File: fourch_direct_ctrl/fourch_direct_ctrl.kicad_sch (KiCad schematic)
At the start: 53 parts, among them J1 Conn_01x04, J10 Conn_01x01, J11 Conn_01x01, J12 Conn_01x01, J13 Conn_01x01, J14 Conn_01x01, J15 Conn_01x01, J16 Conn_01x01, J17 Conn_01x01, J2 Conn_01x02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

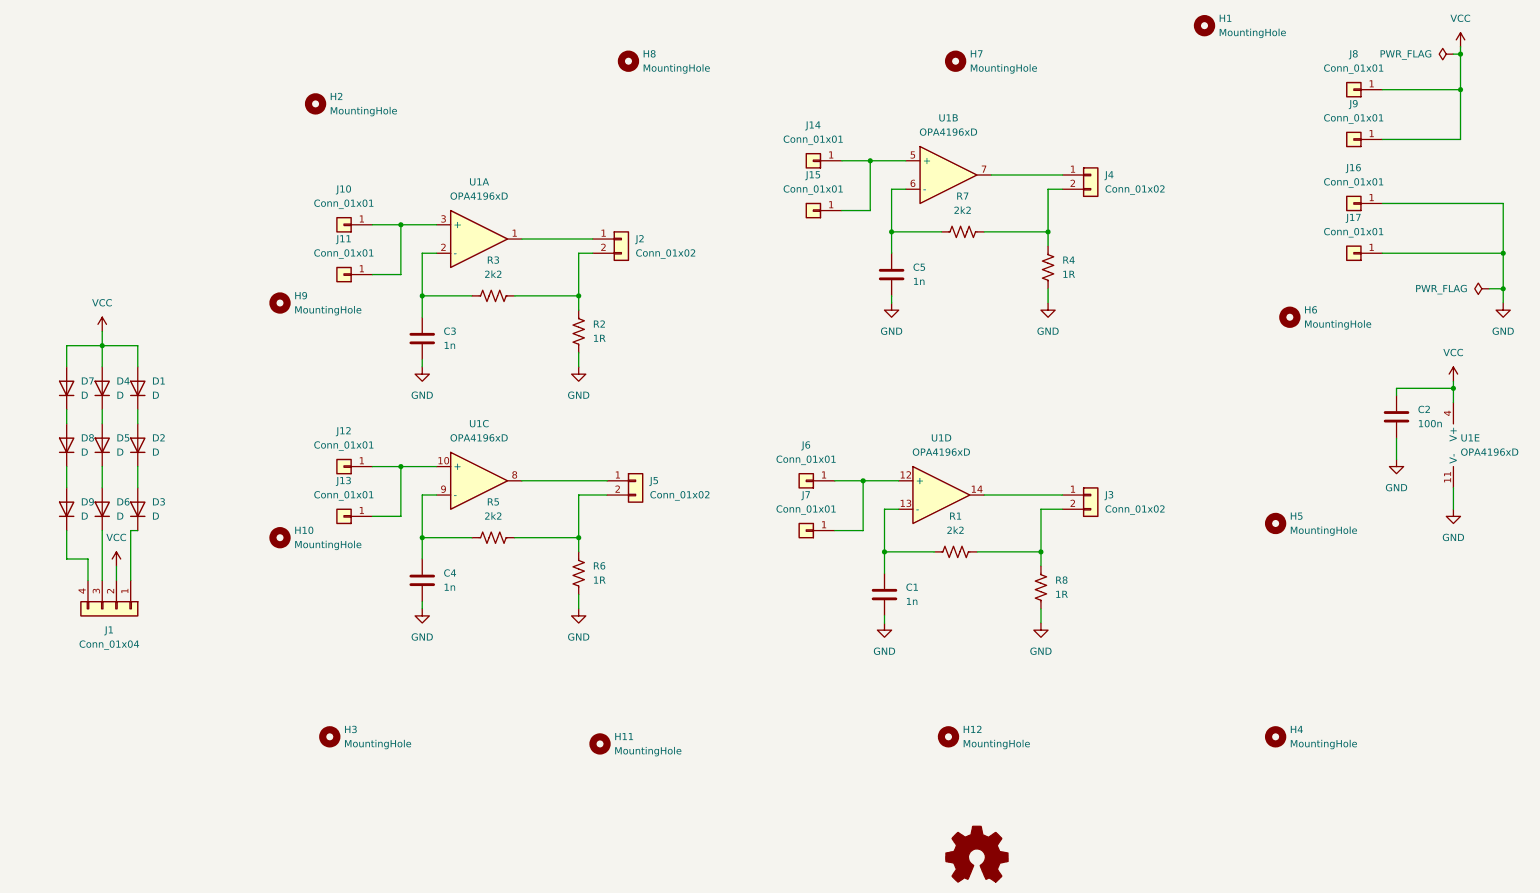
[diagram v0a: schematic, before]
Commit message: rev up fourch lights, add distroboard
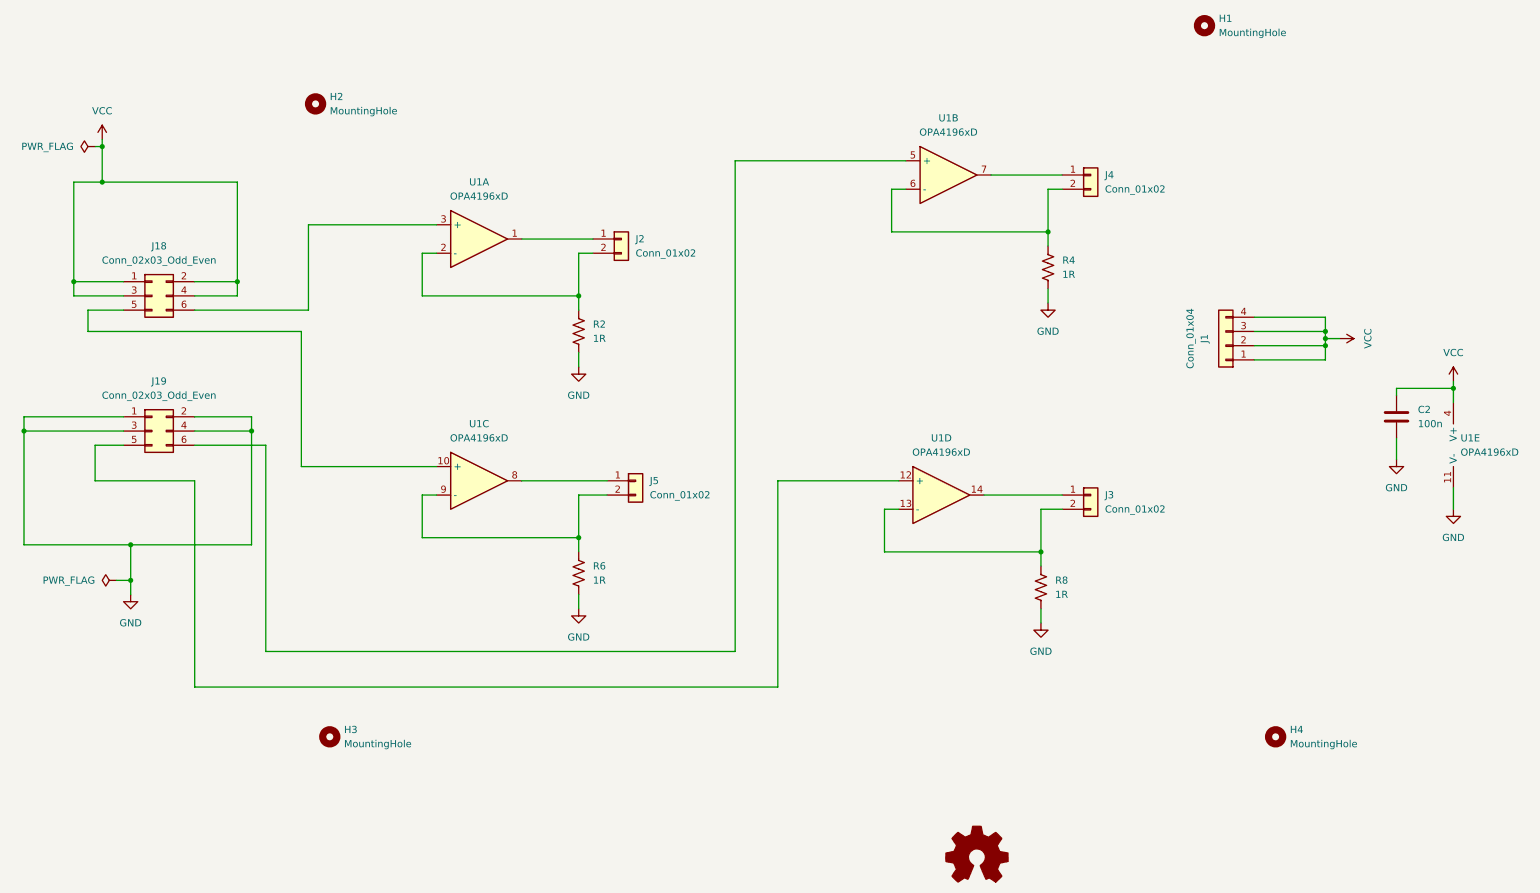
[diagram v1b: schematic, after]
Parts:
- removed C1, C3, C4, C5: 1n, Capacitor_SMD:C_0805_2012Metric_Pad1.18x1.45mm_HandSolder, symbol Device:C
- removed D1, D2, D3, D4, D5, D6, D7, D8, D9: D, Diode_SMD:D_SOD-123F, symbol Device:D
- removed H10, H11, H12, H5, H6, H7, H8, H9: MountingHole, custom_footprints:MountingHole_4.2mm, symbol Mechanical:MountingHole
- removed J10, J11, J12, J13, J14, J15, J6, J7: Conn_01x01, custom_footprints:TE_2834010-3_1x01_P3.0mm_Horizontal, symbol Connector_Generic:Conn_01x01
- removed J16, J17, J8, J9: Conn_01x01, custom_footprints:TE_2834012-3_1x01_P4.0mm_Horizontal, symbol Connector_Generic:Conn_01x01
- removed R1, R3, R5, R7: 2k2, Resistor_SMD:R_0805_2012Metric_Pad1.20x1.40mm_HandSolder, symbol Device:R_US
- added J18, J19: Conn_02x03_Odd_Even, Connector_Wuerth:Wuerth_WR-PHD_610006243021_SMD_2x03_P2.54mm_Vertical, symbol Connector_Generic:Conn_02x03_Odd_Even
- H1, H2, H3, H4: footprint custom_footprints:MountingHole_3.0mm -> custom_footprints:MountingHole_3.45mm
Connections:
- net GND: now also J19.1 (Pin_1), J19.2 (Pin_2), J19.3 (Pin_3), J19.4 (Pin_4)
- net VCC: now also J1.1 (Pin_1), J1.3 (Pin_3), J1.4 (Pin_4), J18.1 (Pin_1), J18.2 (Pin_2), J18.3 (Pin_3), J18.4 (Pin_4)
- net at U1.5 (+): now also J19.6 (Pin_6)
- net at U1.6 (-): now also J4.2 (Pin_2), R4.1
- net at U1.3 (+): now also J18.6 (Pin_6)
- net at U1.13 (-): now also J3.2 (Pin_2), R8.1
- net at U1.10 (+): now also J18.5 (Pin_5)
- net at U1.9 (-): now also J5.2 (Pin_2), R6.1
- net at J2.2 (Pin_2), R2.1: now also U1.2 (-)
- net at U1.12 (+): now also J19.5 (Pin_5)
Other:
- moved on the sheet: J1

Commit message: switch opamps to dual flavors, build in on-board TEC current control
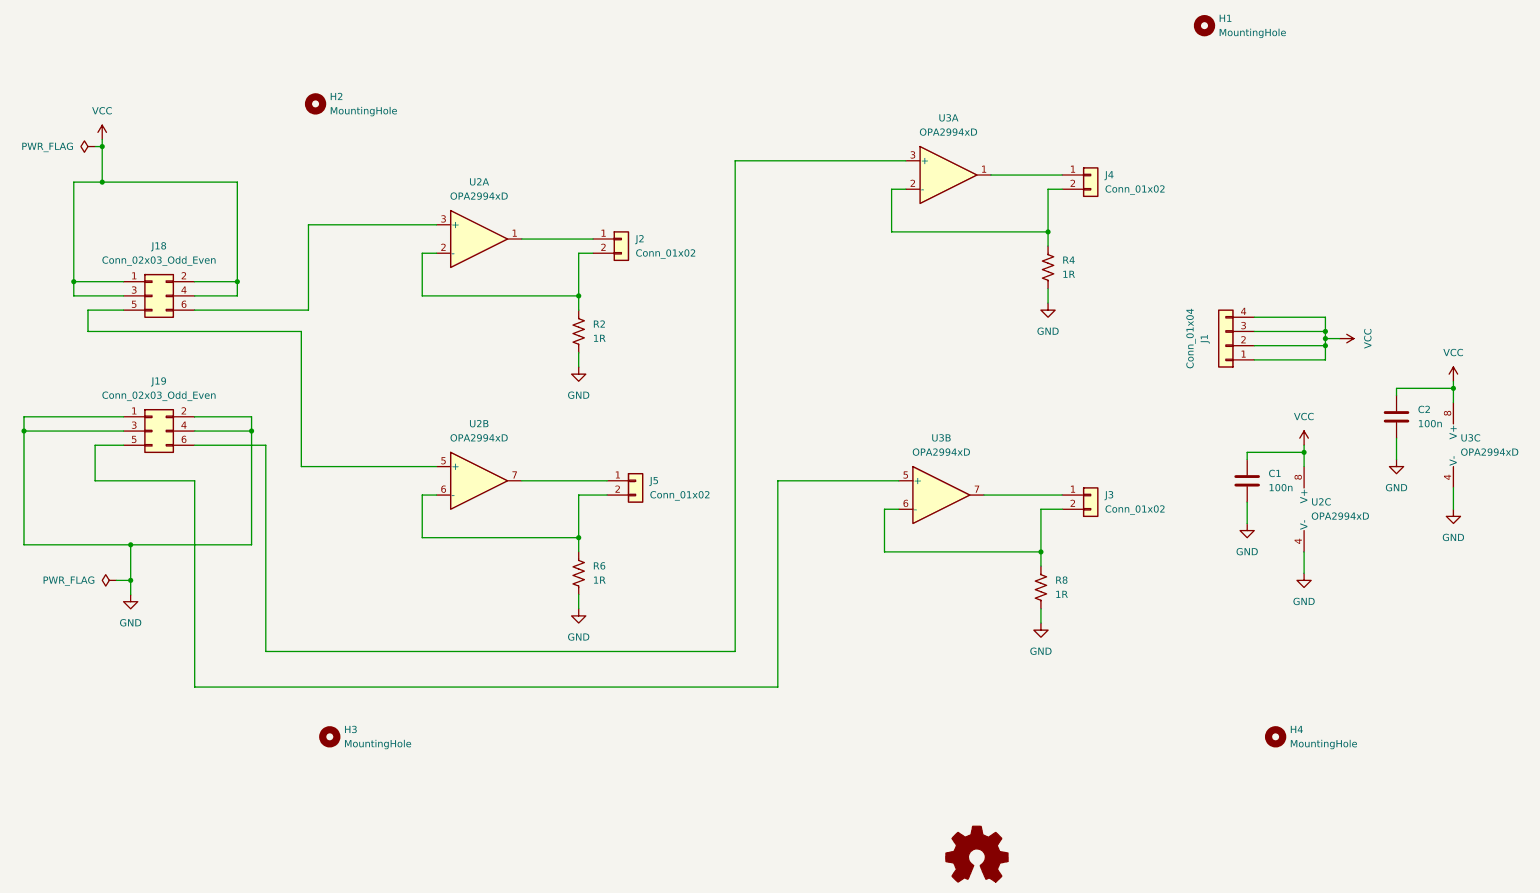
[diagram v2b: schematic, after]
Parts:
- removed U1: OPA4196xD, Package_SO:SOIC-14_3.9x8.7mm_P1.27mm, symbol Amplifier_Operational:OPA4196xD
- added C1: 100n, Capacitor_SMD:C_0805_2012Metric_Pad1.18x1.45mm_HandSolder, symbol Device:C
- added U2, U3: OPA2994xD, Package_SO:SOIC-8_3.9x4.9mm_P1.27mm, symbol Amplifier_Operational:OPA2994xD
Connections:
- net GND: now also C1.2, U2.4 (V-), U3.4 (V-)
- net VCC: now also C1.1, U2.8 (V+), U3.8 (V+)
- net at J19.6 (Pin_6): now also U3.3 (+)
- net at J4.2 (Pin_2), R4.1: now also U3.2 (-)
- net at J4.1 (Pin_1): now also U3.1
- net at J18.5 (Pin_5): now also U2.5 (+)
- net at J5.1 (Pin_1): now also U2.7
- net at J5.2 (Pin_2), R6.1: now also U2.6 (-)
- net at J19.5 (Pin_5): now also U3.5 (+)
- net at J2.1 (Pin_1): now also U2.1
- net at J2.2 (Pin_2), R2.1: now also U2.2 (-)
- net at J18.6 (Pin_6): now also U2.3 (+)
- net at J3.2 (Pin_2), R8.1: now also U3.6 (-)
- net at J3.1 (Pin_1): now also U3.7
